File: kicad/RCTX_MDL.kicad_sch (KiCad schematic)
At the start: 35 parts

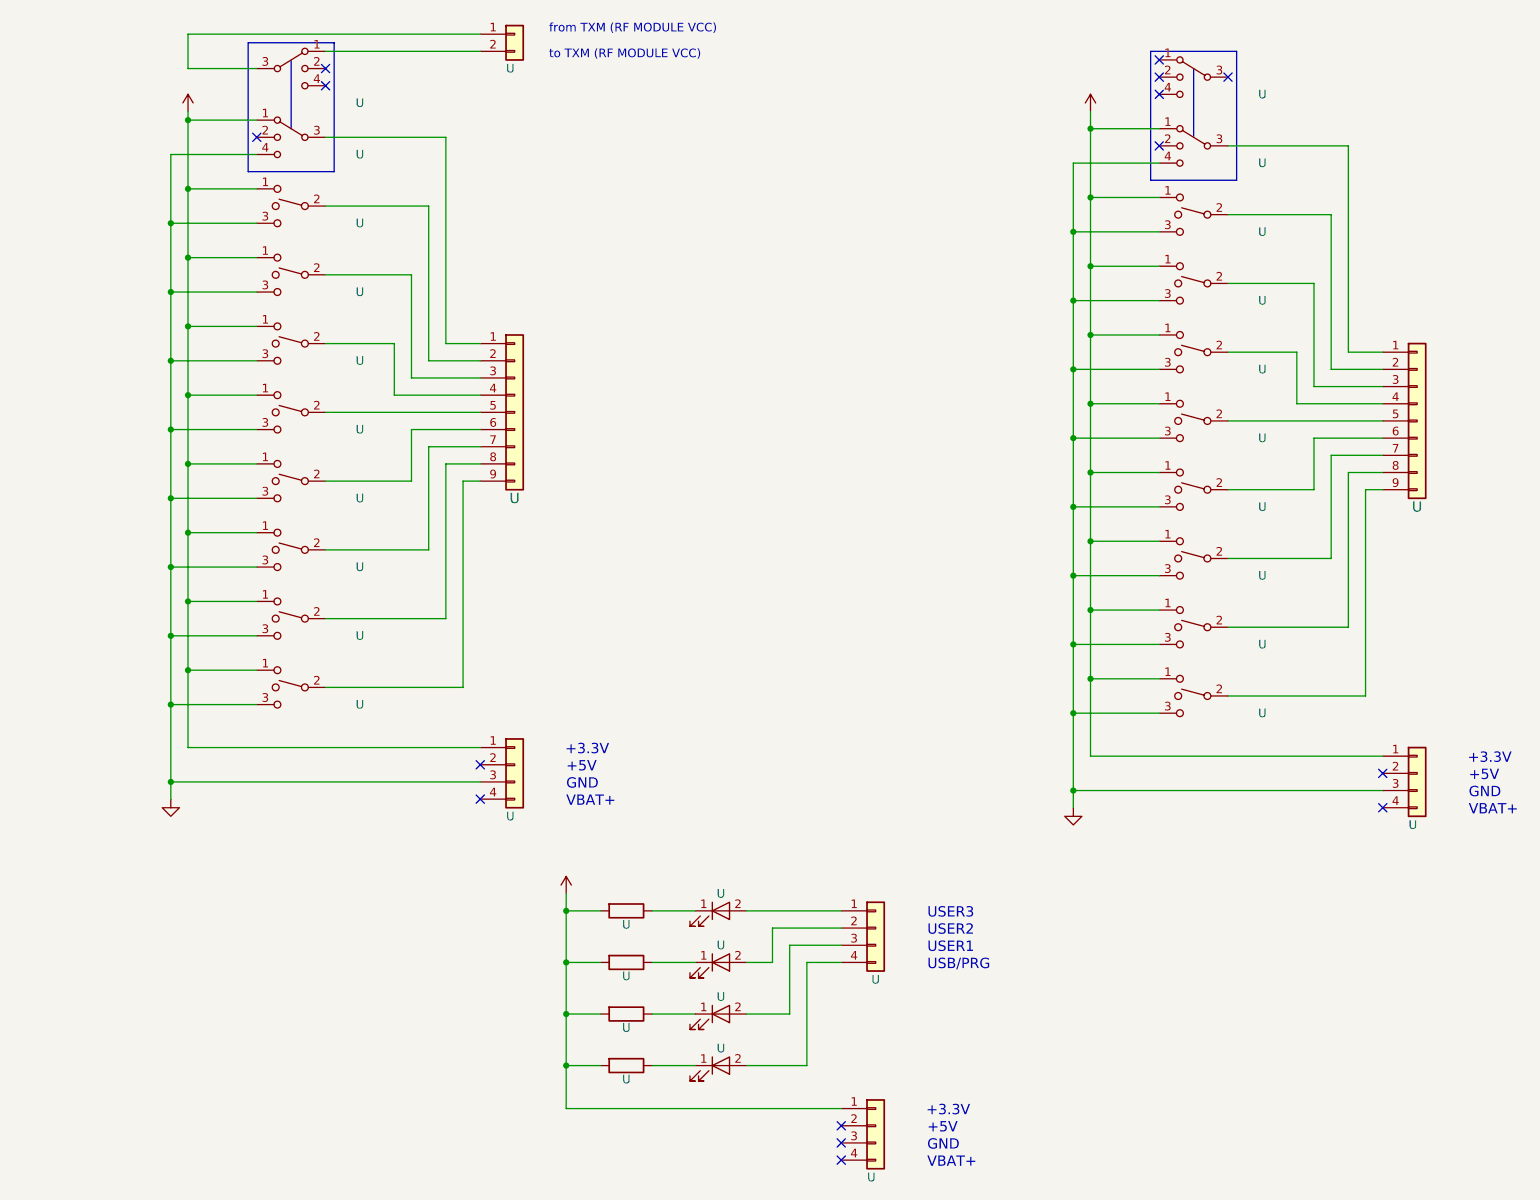
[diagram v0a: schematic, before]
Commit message: Adding PIB USB BRIDGE UML state diagrams - WIP
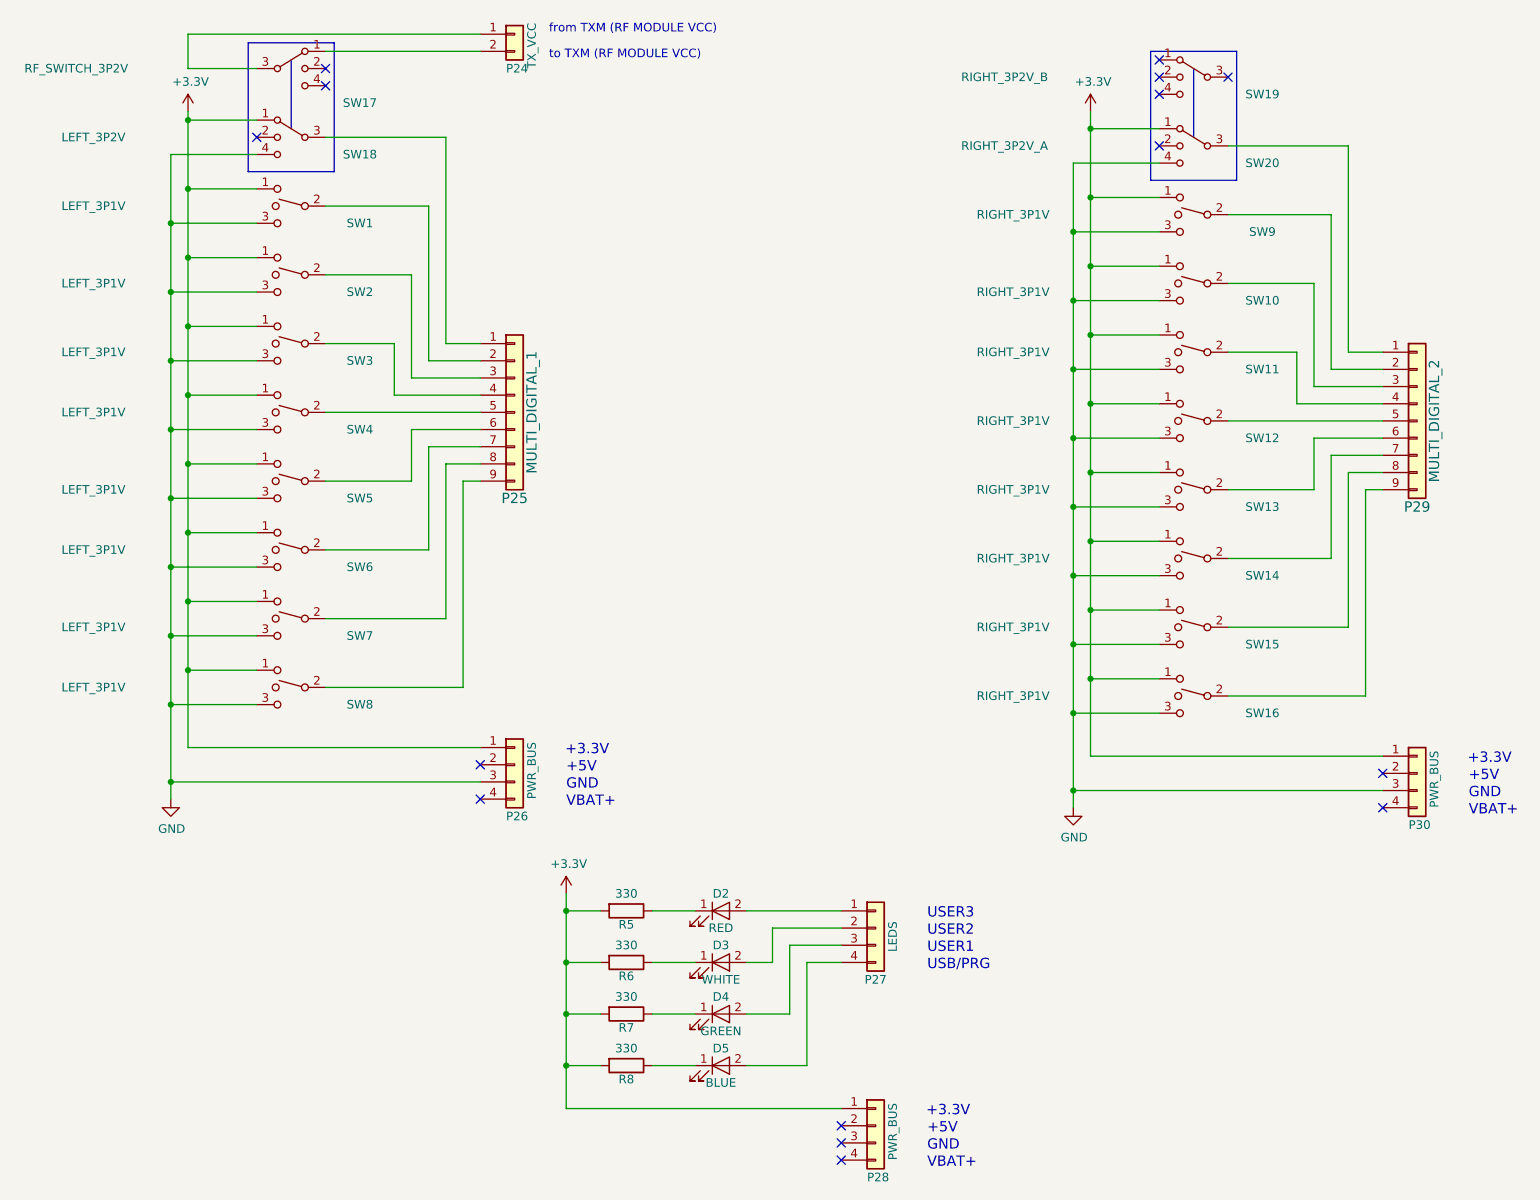
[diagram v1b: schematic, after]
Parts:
- D2: renamed from U; value (none) -> RED; footprint (none) -> LEDs:LED_D3.0mm
- D3: renamed from U; value (none) -> WHITE; footprint (none) -> LEDs:LED_D3.0mm
- D4: renamed from U; value (none) -> GREEN; footprint (none) -> LEDs:LED_D3.0mm
- D5: renamed from U; value (none) -> BLUE; footprint (none) -> LEDs:LED_D3.0mm
- P24: renamed from U; value (none) -> TX_VCC; footprint (none) -> Connectors_Samtec:SL-102-X-XX_1x02
- P25: renamed from U; value (none) -> MULTI_DIGITAL_1; footprint (none) -> Connectors_Samtec:SL-109-X-XX_1x09
- P26, P28, P30: renamed from U; value (none) -> PWR_BUS; footprint (none) -> Connectors_Samtec:SL-104-X-XX_1x04
- P27: renamed from U; value (none) -> LEDS; footprint (none) -> Connectors_Samtec:SL-104-X-XX_1x04
- P29: renamed from U; value (none) -> MULTI_DIGITAL_2; footprint (none) -> Connectors_Samtec:SL-109-X-XX_1x09
- R5, R6, R7, R8: renamed from U; value (none) -> 330; footprint (none) -> Resistors_THT:R_Axial_DIN0204_L3.6mm_D1.6mm_P1.90mm_Vertical
- SW1, SW2, SW3, SW4, SW5, SW6, SW7, SW8: renamed from U; value (none) -> LEFT_3P1V; footprint (none) -> Buttons_Switches_THT:SW_CuK_JS202011CQN_DPDT_Straight
- SW10, SW11, SW12, SW13, SW14, SW15, SW16, SW9: renamed from U; value (none) -> RIGHT_3P1V; footprint (none) -> Buttons_Switches_THT:SW_CuK_JS202011CQN_DPDT_Straight
- SW17: renamed from U; value (none) -> RF_SWITCH_3P2V; footprint (none) -> Buttons_Switches_THT:SW_CuK_JS202011AQN_DPDT_Angled
- SW18: renamed from U; value (none) -> LEFT_3P2V; footprint (none) -> Buttons_Switches_THT:SW_CuK_JS202011AQN_DPDT_Angled
- SW19: renamed from U; value (none) -> RIGHT_3P2V_B; footprint (none) -> Buttons_Switches_THT:SW_CuK_JS202011AQN_DPDT_Angled
- SW20: renamed from U; value (none) -> RIGHT_3P2V_A; footprint (none) -> Buttons_Switches_THT:SW_CuK_JS202011AQN_DPDT_Angled
